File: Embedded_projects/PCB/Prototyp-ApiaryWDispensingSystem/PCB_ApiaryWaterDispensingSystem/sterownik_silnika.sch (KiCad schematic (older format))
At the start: 12 parts

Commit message: added lot of changes to project #3
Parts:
- added R?: 0, Resistor_THT:R_Axial_DIN0204_L3.6mm_D1.6mm_P2.54mm_Vertical, symbol Device:R
- added Wejscie_zasilania_pomp?: Conn_01x02, TerminalBlock_TE-Connectivity:TerminalBlock_TE_282834-2_1x02_P2.54mm_Horizontal, symbol Connector_Generic:Conn_01x02
- C? (x2): footprint (none) -> Capacitor_SMD:C_0805_2012Metric
- JP? (x2): footprint (none) -> Jumper:SolderJumper-2_P1.3mm_Open_TrianglePad1.0x1.5mm
- POMPA_2: footprint (none) -> TerminalBlock_TE-Connectivity:TerminalBlock_TE_282834-2_1x02_P2.54mm_Horizontal
- R? (x2): footprint (none) -> Resistor_SMD:R_0805_2012Metric
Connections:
- net GND: now also R?.2; no longer C?.2, C?.2, R?.2
- net VM: now also C?.1, D?.1 (K), Q?.2 (S), R?.1
- net at Q?.1 (G): now also D?.2 (A), R?.1
- net VIN: now reaches Q?.3 (D)
- net VIN: now also Wejscie_zasilania_pomp?.2 (Pin_2)
- new net GNDA: C?.2, C?.2, R?.1, R?.2, Wejscie_zasilania_pomp?.1 (Pin_1)
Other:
- note added: "Analog Part"
- note added: "Digital PART"
- note added: "Oddzielenie masy cześci analogowej i cyfrowej"
- moved on the sheet: C?, JP?, POMPA_1, POMPA_2, U?

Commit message: Many design changes have been added over the past few months #3
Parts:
- removed R?: 0, Resistor_THT:R_Axial_DIN0204_L3.6mm_D1.6mm_P2.54mm_Vertical, symbol Device:R
- added J?: Conn_02x01, Connector_PinHeader_2.54mm:PinHeader_1x02_P2.54mm_Vertical, symbol Connector_Generic:Conn_02x01
- C? (x2): footprint Capacitor_SMD:C_0805_2012Metric -> Capacitor_SMD:C_0603_1608Metric
- C?: footprint (none) -> Capacitor_SMD:C_0805_2012Metric
- D?: value D_Schottky 6,8 V -> D_Schottky 6,8 V SMAZ6V8; footprint (none) -> Diode_SMD:D_SMA
- POMPA_1: footprint (none) -> TerminalBlock_TE-Connectivity:TerminalBlock_TE_282834-2_1x02_P2.54mm_Horizontal
- Q?: footprint (none) -> Package_TO_SOT_SMD:SOT-23
- R? (x2): footprint Resistor_SMD:R_0805_2012Metric -> Resistor_SMD:R_0603_1608Metric
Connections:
- net GND: now also J?.1 (Pin_1)
- net GNDA: now also J?.2 (Pin_2)
- net +3V3 renamed VDD
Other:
- note added: "Tranzystor P-MOSFET FDN338P SOT23"
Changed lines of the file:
@@
 $Descr A4 11693 8268
 encoding utf-8
-Sheet 5 9
+Sheet 4 9
 Title ""
 Date ""
@@
 F 0 "POMPA_1" H 778 2225 50  0000 C CNN
 F 1 "Conn_01x02" H 778 2316 50  0000 C CNN
-F 2 "" H 860 2550 50  0001 C CNN
+F 2 "TerminalBlock_TE-Connectivity:TerminalBlock_TE_282834-2_1x02_P2.54mm_Horizontal" H 860 2550 50  0001 C CNN
 F 3 "~" H 860 2550 50  0001 C CNN
 	1    860  2550
@@
 	3170 2800 3170 3050
 Text GLabel 5280 2400 2    50   Input ~ 0
-BENBL
+BENABLE
 Text GLabel 5270 2500 2    50   Input ~ 0
 BPHASE
@@
 BPHASE
 Text HLabel 890  900  0    50   Input ~ 0
-AENBL
+AENABLE
 Text HLabel 890  700  0    50   Input ~ 0
-BENBL
+BENABLE
 Text HLabel 890  1100 0    50   Input ~ 0
 MODE
 Text GLabel 1090 700  2    50   Input ~ 0
-BENBL
+BENABLE
 Text GLabel 1090 790  2    50   Input ~ 0
 BPHASE
 Text GLabel 1090 900  2    50   Input ~ 0
-AENBL
+AENABLE
 Text GLabel 1090 1000 2    50   Input ~ 0
 APHASE
@@
 MOSTKOWANIE
 $Comp
-L power:+3V3 #PWR0165
-U 1 1 67E398B8
-P 4550 1410
-F 0 "#PWR0165" H 4550 1260 50  0001 C CNN
-F 1 "+3V3" H 4565 1583 50  0000 C CNN
-F 2 "" H 4550 1410 50  0001 C CNN
-F 3 "" H 4550 1410 50  0001 C CNN
-	1    4550 1410
-	1    0    0    -1
-$EndComp
-$Comp
 L power:GND #PWR0166
 U 1 1 67E3A3D8
@@
 F 0 "C?" H 4935 1766 50  0000 L CNN
 F 1 "100n" H 4935 1675 50  0000 L CNN
-F 2 "Capacitor_SMD:C_0805_2012Metric" H 4858 1570 50  0001 C CNN
+F 2 "Capacitor_SMD:C_0603_1608Metric" H 4858 1570 50  0001 C CNN
 F 3 "~" H 4820 1720 50  0001 C CNN
 	1    4820 1720
@@
 P 7400 1150
 F 0 "D?" V 7354 1230 50  0000 L CNN
-F 1 "D_Schottky 6,8 V" V 7540 1050 50  0000 L CNN
-F 2 "" H 7400 1150 50  0001 C CNN
+F 1 "D_Schottky 6,8 V SMAZ6V8" V 7430 -270 50  0000 L CNN
+F 2 "Diode_SMD:D_SMA" H 7400 1150 50  0001 C CNN
 F 3 "~" H 7400 1150 50  0001 C CNN
 	1    7400 1150
@@
 F 0 "R?" H 7470 1616 50  0000 L CNN
 F 1 "100k" H 7470 1525 50  0000 L CNN
-F 2 "Resistor_SMD:R_0805_2012Metric" V 7330 1570 50  0001 C CNN
+F 2 "Resistor_SMD:R_0603_1608Metric" V 7330 1570 50  0001 C CNN
 F 3 "~" H 7400 1570 50  0001 C CNN
 	1    7400 1570
@@
 F 0 "R?" H 8170 1186 50  0000 L CNN
 F 1 "1" H 8170 1095 50  0000 L CNN
-F 2 "Resistor_SMD:R_0805_2012Metric" V 8030 1140 50  0001 C CNN
+F 2 "Resistor_SMD:R_0603_1608Metric" V 8030 1140 50  0001 C CNN
 F 3 "~" H 8100 1140 50  0001 C CNN
 	1    8100 1140
@@
 F 0 "C?" H 8215 1586 50  0000 L CNN
 F 1 "10u" H 8215 1495 50  0000 L CNN
-F 2 "" H 8138 1390 50  0001 C CNN
+F 2 "Capacitor_SMD:C_0805_2012Metric" H 8138 1390 50  0001 C CNN
 F 3 "~" H 8100 1540 50  0001 C CNN
 	1    8100 1540
@@
 F 0 "C?" H 8615 1196 50  0000 L CNN
 F 1 "100n" H 8615 1105 50  0000 L CNN
-F 2 "Capacitor_SMD:C_0805_2012Metric" H 8538 1000 50  0001 C CNN
+F 2 "Capacitor_SMD:C_0603_1608Metric" H 8538 1000 50  0001 C CNN
 F 3 "~" H 8500 1150 50  0001 C CNN
 	1    8500 1150
@@
 F 0 "Q?" V 7422 1010 50  0000 C CNN
 F 1 "Q_PMOS_GSD" V 7331 1010 50  0000 C CNN
-F 2 "" H 7280 1110 50  0001 C CNN
+F 2 "Package_TO_SOT_SMD:SOT-23" H 7280 1110 50  0001 C CNN
 F 3 "~" H 7080 1010 50  0001 C CNN
 	1    7080 1010
@@
 Wire Wire Line
 	8500 1300 8500 1930
-Text Notes 760  4170 0    79   ~ 0
+Text Notes 745  4075 0    79   ~ 0
 Oddzielenie masy cześci analogowej i cyfrowej
 $Comp
@@
 Wire Wire Line
 	1080 3690 1450 3690
-$Comp
-L Device:R R?
-U 1 1 67FBCED9
-P 1800 4410
-F 0 "R?" V 1700 4290 50  0000 L CNN
-F 1 "0" V 1700 4480 50  0000 L CNN
-F 2 "Resistor_THT:R_Axial_DIN0204_L3.6mm_D1.6mm_P2.54mm_Vertical" V 1730 4410 50  0001 C CNN
-F 3 "~" H 1800 4410 50  0001 C CNN
-	1    1800 4410
-	0    1    1    0
-$EndComp
-Wire Wire Line
-	1950 4410 2180 4410
-Wire Wire Line
-	2180 4410 2180 4530
-Wire Wire Line
-	1650 4410 1470 4410
-Wire Wire Line
-	1470 4410 1470 4520
 Text Notes 2560 1960 0    50   ~ 0
 Digital PART
@@
 Analog Part
 Wire Wire Line
-	4550 1410 4550 1500
-Wire Wire Line
 	4820 1980 4820 1870
 Wire Wire Line
@@
 Wire Wire Line
 	4550 1500 4550 2200
+$Comp
+L Connector_Generic:Conn_02x01 J?
+U 1 1 68EF4B8A
+P 1720 4335
+F 0 "J?" H 1760 4215 50  0000 C CNN
+F 1 "Conn_02x01" H 1770 4461 50  0000 C CNN
+F 2 "Connector_PinHeader_2.54mm:PinHeader_1x02_P2.54mm_Vertical" H 1720 4335 50  0001 C CNN
+F 3 "~" H 1720 4335 50  0001 C CNN
+	1    1720 4335
+	1    0    0    -1
+$EndComp
+Wire Wire Line
+	1470 4335 1520 4335
+Wire Wire Line
+	1470 4335 1470 4520
+Wire Wire Line
+	2020 4335 2180 4335
+Wire Wire Line
+	2180 4335 2180 4530
+Text Notes 5260 785  0    50   ~ 0
+Tranzystor P-MOSFET FDN338P SOT23
+$Comp
+L power:VDD #PWR?
+U 1 1 68F93D47
+P 4550 1350
+F 0 "#PWR?" H 4550 1200 50  0001 C CNN
+F 1 "VDD" H 4565 1523 50  0000 C CNN
+F 2 "" H 4550 1350 50  0001 C CNN
+F 3 "" H 4550 1350 50  0001 C CNN
+	1    4550 1350
+	1    0    0    -1
+$EndComp
+Wire Wire Line
+	4550 1350 4550 1500
+Text GLabel 1090 1225 2    50   Input ~ 0
+VM
+Text HLabel 870  1225 0    50   Input ~ 0
+VM
+Wire Wire Line
+	1090 1225 870  1225
 $EndSCHEMATC

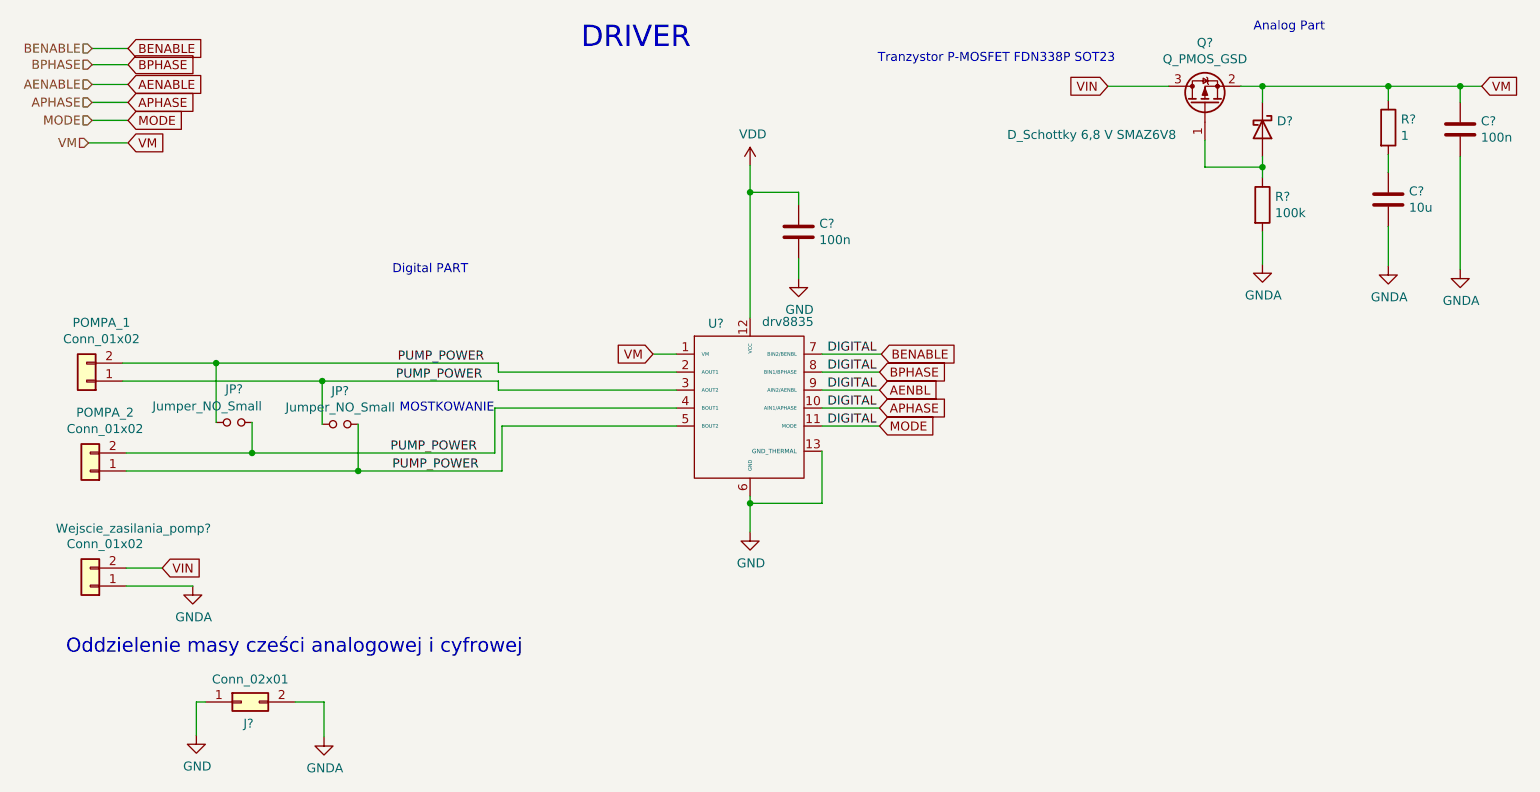
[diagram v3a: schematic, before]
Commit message: All signal has been routed, the analog part needs to be completed
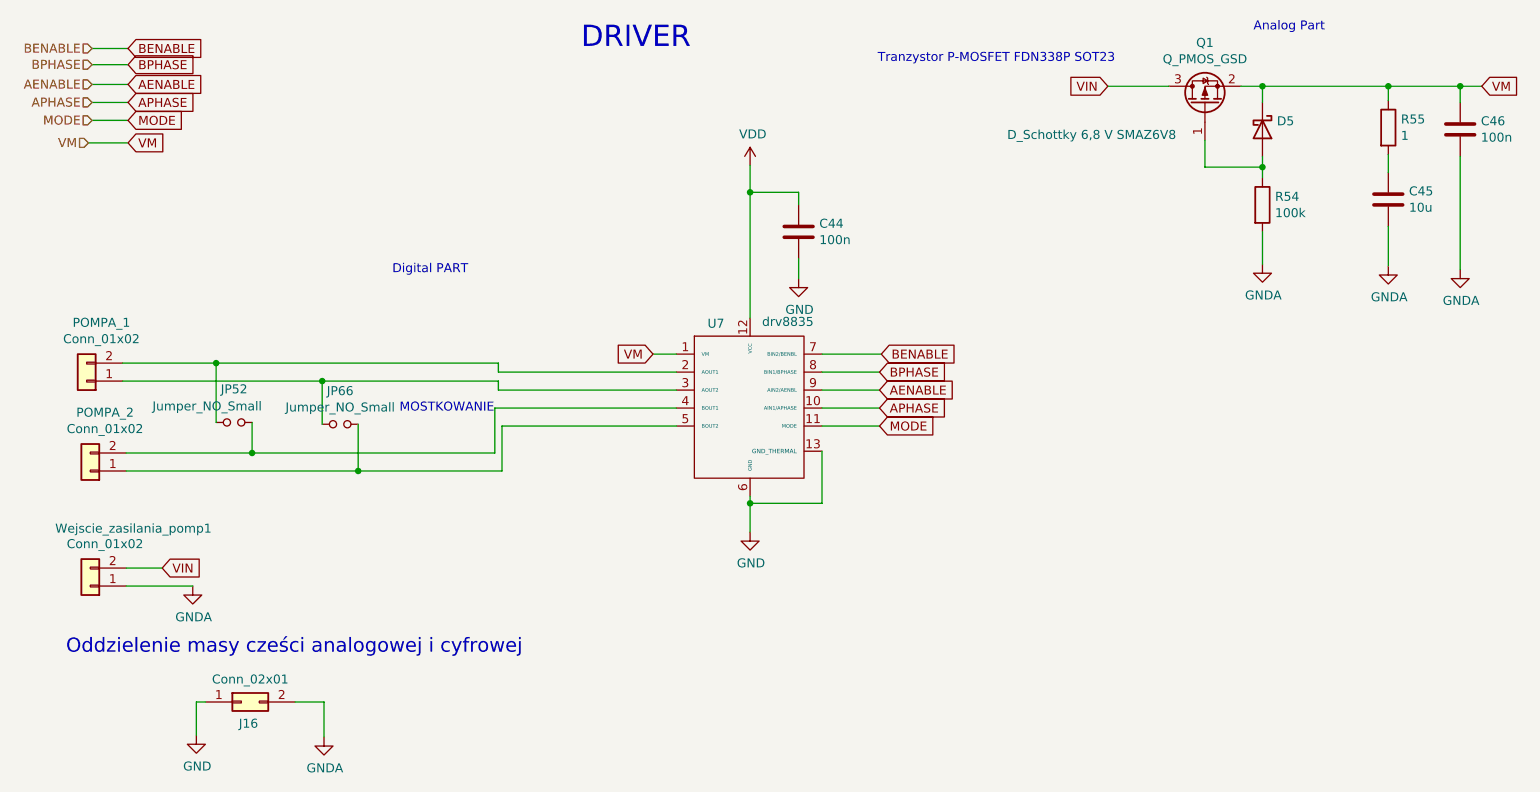
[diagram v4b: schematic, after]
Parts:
- U7: renamed from U?; footprint (none) -> Package_SON:WSON-12-1EP_3x2mm_P0.5mm_EP1x2.65_ThermalVias
- gave numbers to parts that had none: 11
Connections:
- net AENABLE: now also U7.9 (AIN2/AENBL)
- removed net AENBL: U7.10 (AIN1/APHASE), U7.11 (MODE), U7.7 (BIN2/BENBL), U7.8 (BIN1/BPHASE), U7.9 (AIN2/AENBL)
- removed net PUMP_POWER: JP52.1, JP52.2, JP66.1, JP66.2, POMPA_1.1 (Pin_1), POMPA_1.2 (Pin_2), POMPA_2.1 (Pin_1), POMPA_2.2 (Pin_2), U7.2 (AOUT1), U7.3 (AOUT2), U7.4 (BOUT1), U7.5 (BOUT2)
- new net: JP66.1, POMPA_1.1 (Pin_1), U7.3 (AOUT2)
- new net: JP52.1, POMPA_1.2 (Pin_2), U7.2 (AOUT1)
- new net: JP66.2, POMPA_2.1 (Pin_1), U7.5 (BOUT2)
- new net: JP52.2, POMPA_2.2 (Pin_2), U7.4 (BOUT1)
- new net APHASE: U7.10 (AIN1/APHASE)
- new net BENABLE: U7.7 (BIN2/BENBL)
- new net BPHASE: U7.8 (BIN1/BPHASE)
- new net MODE: U7.11 (MODE)
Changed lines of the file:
@@
 	3150 2600 3150 2550
 $Comp
-L library-ApiaryWater:drv8835 U?
+L library-ApiaryWater:drv8835 U7
 U 1 1 67E33780
 P 4550 2700
-F 0 "U?" H 4360 3170 50  0000 C CNN
+F 0 "U7" H 4360 3170 50  0000 C CNN
 F 1 "drv8835" H 4760 3180 50  0000 C CNN
-F 2 "" H 4550 2700 50  0001 C CNN
+F 2 "Package_SON:WSON-12-1EP_3x2mm_P0.5mm_EP1x2.65_ThermalVias" H 4550 2700 50  0001 C CNN
 F 3 "" H 4550 2700 50  0001 C CNN
 	1    4550 2700
@@
 Text GLabel 5270 2500 2    50   Input ~ 0
 BPHASE
-Text GLabel 5270 2600 2    50   Input ~ 0
-AENBL
 Text GLabel 5270 2700 2    50   Input ~ 0
 APHASE
@@
 Text Notes 3610 710  0    118  ~ 0
 DRIVER
-Text Label 2590 2450 0    50   ~ 0
-PUMP_POWER
-Text Label 2580 2550 0    50   ~ 0
-PUMP_POWER
-Text Label 2550 2950 0    50   ~ 0
-PUMP_POWER
-Text Label 2560 3050 0    50   ~ 0
-PUMP_POWER
-Text Label 4980 2400 0    50   ~ 0
-DIGITAL
 Wire Wire Line
 	4950 2400 5280 2400
@@
 Wire Wire Line
 	4950 2800 5270 2800
-Text Label 4980 2500 0    50   ~ 0
-DIGITAL
-Text Label 4980 2600 0    50   ~ 0
-DIGITAL
-Text Label 4980 2700 0    50   ~ 0
-DIGITAL
-Text Label 4980 2800 0    50   ~ 0
-DIGITAL
-$Comp
-L Device:Jumper_NO_Small JP?
+$Comp
+L Device:Jumper_NO_Small JP52
 U 1 1 67E30C26
 P 1680 2780
-F 0 "JP?" H 1680 2965 50  0000 C CNN
+F 0 "JP52" H 1680 2965 50  0000 C CNN
 F 1 "Jumper_NO_Small" H 1530 2870 50  0000 C CNN
 F 2 "Jumper:SolderJumper-2_P1.3mm_Open_TrianglePad1.0x1.5mm" H 1680 2780 50  0001 C CNN
@@
 $EndComp
 $Comp
-L Device:Jumper_NO_Small JP?
+L Device:Jumper_NO_Small JP66
 U 1 1 67E3150B
 P 2270 2790
-F 0 "JP?" H 2270 2975 50  0000 C CNN
+F 0 "JP66" H 2270 2975 50  0000 C CNN
 F 1 "Jumper_NO_Small" H 2270 2884 50  0000 C CNN
 F 2 "Jumper:SolderJumper-2_P1.3mm_Open_TrianglePad1.0x1.5mm" H 2270 2790 50  0001 C CNN
@@
 $EndComp
 $Comp
-L Device:C C?
+L Device:C C44
 U 1 1 67E3B4B9
 P 4820 1720
-F 0 "C?" H 4935 1766 50  0000 L CNN
+F 0 "C44" H 4935 1766 50  0000 L CNN
 F 1 "100n" H 4935 1675 50  0000 L CNN
 F 2 "Capacitor_SMD:C_0603_1608Metric" H 4858 1570 50  0001 C CNN
@@
 VM
 $Comp
-L Device:D_Schottky D?
+L Device:D_Schottky D5
 U 1 1 67E41C38
 P 7400 1150
-F 0 "D?" V 7354 1230 50  0000 L CNN
+F 0 "D5" V 7354 1230 50  0000 L CNN
 F 1 "D_Schottky 6,8 V SMAZ6V8" V 7430 -270 50  0000 L CNN
 F 2 "Diode_SMD:D_SMA" H 7400 1150 50  0001 C CNN
@@
 $EndComp
 $Comp
-L Device:R R?
+L Device:R R54
 U 1 1 67E428F8
 P 7400 1570
-F 0 "R?" H 7470 1616 50  0000 L CNN
+F 0 "R54" H 7470 1616 50  0000 L CNN
 F 1 "100k" H 7470 1525 50  0000 L CNN
 F 2 "Resistor_SMD:R_0603_1608Metric" V 7330 1570 50  0001 C CNN
@@
 $EndComp
 $Comp
-L Device:R R?
+L Device:R R55
 U 1 1 67E42C3E
 P 8100 1140
-F 0 "R?" H 8170 1186 50  0000 L CNN
+F 0 "R55" H 8170 1186 50  0000 L CNN
 F 1 "1" H 8170 1095 50  0000 L CNN
 F 2 "Resistor_SMD:R_0603_1608Metric" V 8030 1140 50  0001 C CNN
@@
 $EndComp
 $Comp
-L Device:C C?
+L Device:C C45
 U 1 1 67E4304B
 P 8100 1540
-F 0 "C?" H 8215 1586 50  0000 L CNN
+F 0 "C45" H 8215 1586 50  0000 L CNN
 F 1 "10u" H 8215 1495 50  0000 L CNN
 F 2 "Capacitor_SMD:C_0805_2012Metric" H 8138 1390 50  0001 C CNN
@@
 $EndComp
 $Comp
-L Device:C C?
+L Device:C C46
 U 1 1 67E439CE
 P 8500 1150
-F 0 "C?" H 8615 1196 50  0000 L CNN
+F 0 "C46" H 8615 1196 50  0000 L CNN
 F 1 "100n" H 8615 1105 50  0000 L CNN
 F 2 "Capacitor_SMD:C_0603_1608Metric" H 8538 1000 50  0001 C CNN
@@
 	4550 3230 4550 3390
 $Comp
-L Device:Q_PMOS_GSD Q?
+L Device:Q_PMOS_GSD Q1
 U 1 1 67E3DE47
 P 7080 1010
-F 0 "Q?" V 7422 1010 50  0000 C CNN
+F 0 "Q1" V 7422 1010 50  0000 C CNN
 F 1 "Q_PMOS_GSD" V 7331 1010 50  0000 C CNN
 F 2 "Package_TO_SOT_SMD:SOT-23" H 7280 1110 50  0001 C CNN
@@
 	6540 910  6880 910
 $Comp
-L Connector_Generic:Conn_01x02 Wejscie_zasilania_pomp?
+L Connector_Generic:Conn_01x02 Wejscie_zasilania_pomp1
 U 1 1 67FB261B
 P 880 3690
-F 0 "Wejscie_zasilania_pomp?" H 640 3370 50  0000 C CNN
+F 0 "Wejscie_zasilania_pomp1" H 640 3370 50  0000 C CNN
 F 1 "Conn_01x02" H 798 3456 50  0000 C CNN
 F 2 "TerminalBlock_TE-Connectivity:TerminalBlock_TE_282834-2_1x02_P2.54mm_Horizontal" H 880 3690 50  0001 C CNN
@@
 	4550 1500 4550 2200
 $Comp
-L Connector_Generic:Conn_02x01 J?
+L Connector_Generic:Conn_02x01 J16
 U 1 1 68EF4B8A
 P 1720 4335
-F 0 "J?" H 1760 4215 50  0000 C CNN
+F 0 "J16" H 1760 4215 50  0000 C CNN
 F 1 "Conn_02x01" H 1770 4461 50  0000 C CNN
 F 2 "Connector_PinHeader_2.54mm:PinHeader_1x02_P2.54mm_Vertical" H 1720 4335 50  0001 C CNN
@@
 Tranzystor P-MOSFET FDN338P SOT23
 $Comp
-L power:VDD #PWR?
+L power:VDD #PWR026
 U 1 1 68F93D47
 P 4550 1350
-F 0 "#PWR?" H 4550 1200 50  0001 C CNN
+F 0 "#PWR026" H 4550 1200 50  0001 C CNN
 F 1 "VDD" H 4565 1523 50  0000 C CNN
 F 2 "" H 4550 1350 50  0001 C CNN
@@
 Wire Wire Line
 	1090 1225 870  1225
+Text GLabel 5270 2600 2    50   Input ~ 0
+AENABLE
 $EndSCHEMATC
